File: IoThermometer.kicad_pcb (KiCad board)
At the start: 2 copper layers, 80 x 33 mm, 10 parts, among them U1 NodeMCU_Amica_R2

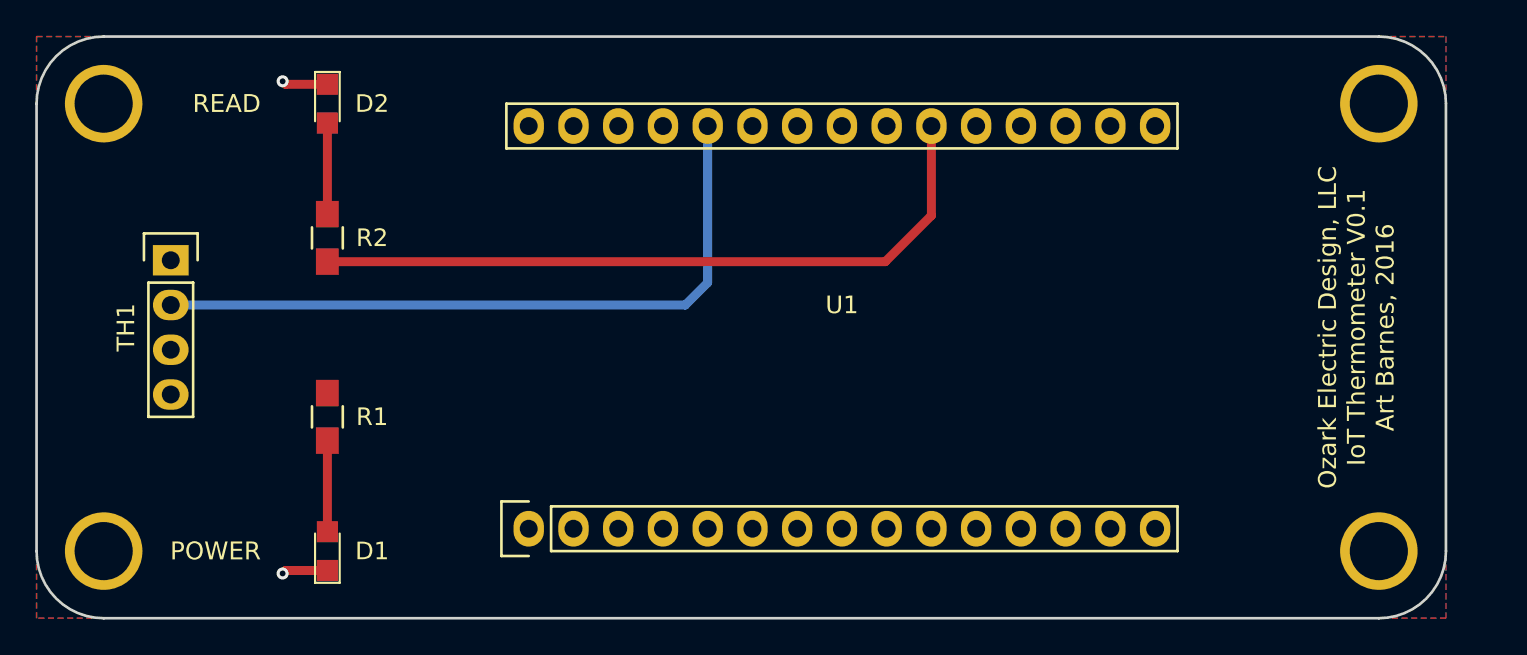
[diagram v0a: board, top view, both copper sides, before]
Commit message: adjusted pcb size
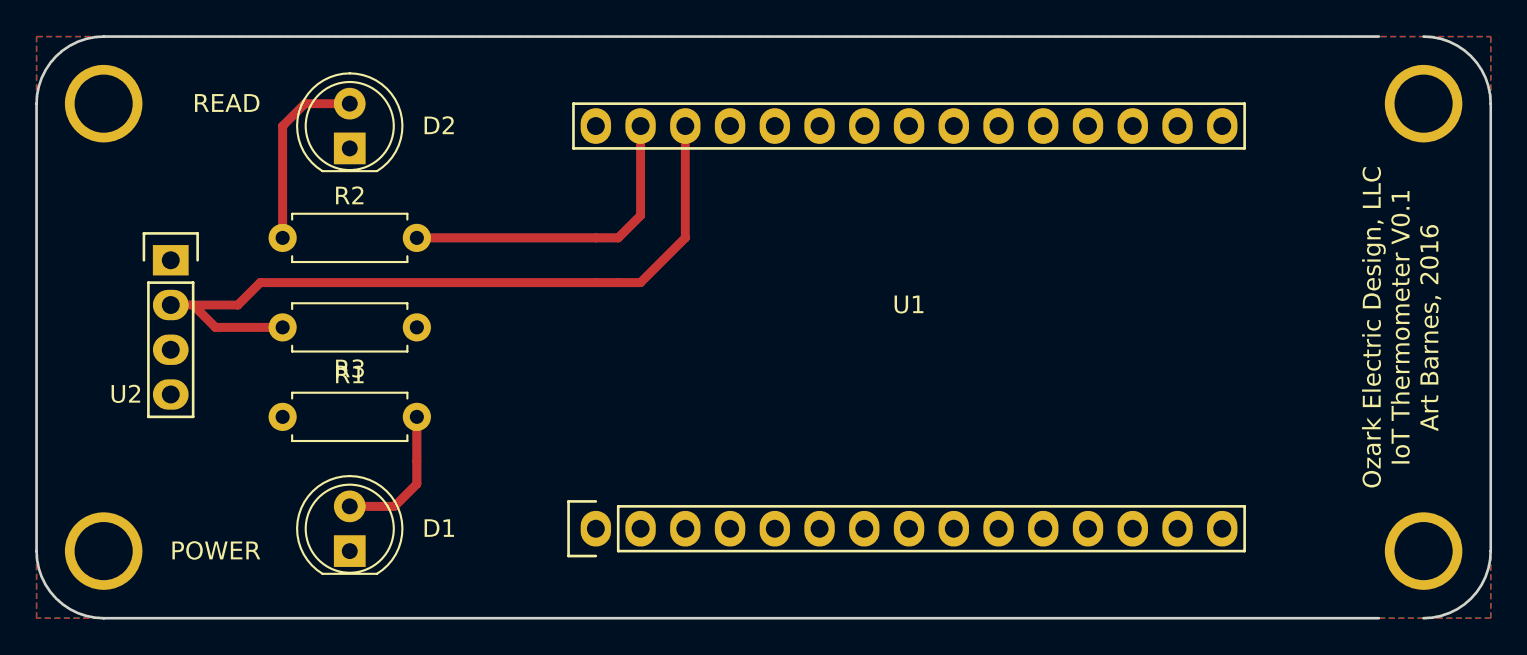
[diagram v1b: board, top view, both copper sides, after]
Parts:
- removed TH1: DHT22_Temperature_Humidity, Sensors:DHT22_Temperature_Humidity
- added R3: 4.7k, Resistor_THT:R_Axial_DIN0207_L6.3mm_D2.5mm_P7.62mm_Horizontal, F.Cu at (126.8, 107.6)
- added U2: DS18B20, Sensors:DHT22_Temperature_Humidity, F.Cu at (112.8, 107.6)
- D1, D2: footprint LEDs:LED_0805 -> LED_THT:LED_D5.0mm
- R1, R2: footprint Resistors_SMD:R_0805_HandSoldering -> Resistor_THT:R_Axial_DIN0207_L6.3mm_D2.5mm_P7.62mm_Horizontal
- moved U1 3.81 mm to (137.0, 119.0)
- moved D2 2.84 mm to (123.0, 97.4), turned to 90 degrees
- moved REF** 2.54 mm to (184.0, 120.3)
- moved REF** 2.54 mm to (184.0, 94.9)
- moved R1 2.54 mm to (119.2, 112.7), turned to 0 degrees
- moved R2 2.54 mm to (119.2, 102.5), turned to 0 degrees
- moved D1 1.27 mm to (123.0, 120.3)
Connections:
- U1 pad 21: Net-(R2-Pad2) -> Net-(U1-Pad21)
- U1 pad 29: Net-(U1-Pad29) -> Net-(R2-Pad2)
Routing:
- net Net-(R3-Pad2): track 0.00 -> 42.7 mm
- net Net-(U1-Pad26): track 39.9 -> 0.00 mm
- net Net-(R2-Pad2): track 40.5 -> 18.3 mm
- net Net-(D2-Pad2): track 5.17 -> 10.7 mm
- net GND: track 5.22 -> 0.00 mm, vias 2 -> 0
- net Net-(D1-Pad2): track 5.17 -> 8.15 mm
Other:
- board size 80 x 33 mm -> 82.6 x 33 mm
